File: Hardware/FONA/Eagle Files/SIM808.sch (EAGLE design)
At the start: 28 parts, among them SW1 KMR2, SW2 KMR2, X2 uFL, X3 uFL, X6 SIM_LOCKAMPHENOL

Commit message: Corrige el esquemático para el SIM808
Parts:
- removed R4, R6: 10K, microbuilder:RESISTOR0805_NOOUTLINE
- removed X2: uFL, microbuilder:SMACONNECTOR_EDGE_UFL
- added D7: 1N4148, microbuilder:DIODESOD-323
- added R1: 10K, microbuilder:RESISTOR0805_NOOUTLINE
- added X1: uFL, microbuilder:ANTENNA_U.FL
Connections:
- new net N$2: D7.A, U1.RI
- new net RI_P: D7.C, R1.2
- net GND: now also R1.1, X1.GND@0, X1.GND@1; no longer R4.1, R6.1, X2.GND1, X2.GND2, X2.GND3, X2.GND4
- net N$16: now also X1.SIGNAL; no longer X2.ANT
- net NS_P: no longer R4.2
- net PS_P: no longer R6.2
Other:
- moved on the sheet: D1, D3, D4, R2, R7, SW1, SW2

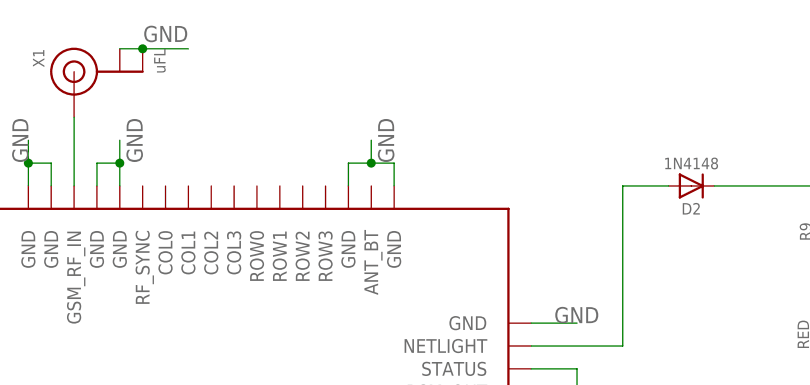
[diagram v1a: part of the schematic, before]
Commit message: Agrega antena para BT en SIM808
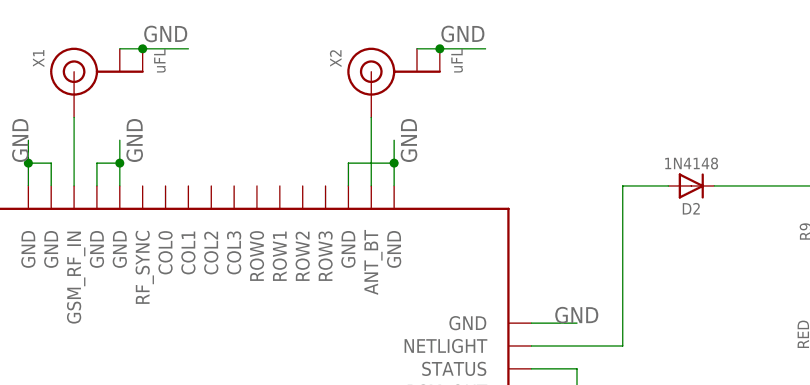
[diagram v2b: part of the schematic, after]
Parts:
- added X2: uFL, microbuilder:ANTENNA_U.FL
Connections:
- new net N$4: X2.SIGNAL
- net GND: now also X2.GND@0, X2.GND@1
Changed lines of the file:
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@@
 <grid distance="0.1" unitdist="inch" unit="inch" style="lines" multiple="1" display="no" altdistance="0.01" altunitdist="inch" altunit="inch"/>
 <layers>
-<layer number="1" name="Top" color="4" fill="1" visible="yes" active="no"/>
-<layer number="16" name="Bottom" color="1" fill="1" visible="yes" active="no"/>
-<layer number="17" name="Pads" color="2" fill="1" visible="yes" active="no"/>
-<layer number="18" name="Vias" color="2" fill="1" visible="yes" active="no"/>
-<layer number="19" name="Unrouted" color="6" fill="1" visible="yes" active="no"/>
-<layer number="20" name="Dimension" color="15" fill="1" visible="yes" active="no"/>
-<layer number="21" name="tPlace" color="7" fill="1" visible="yes" active="no"/>
-<layer number="22" name="bPlace" color="7" fill="1" visible="yes" active="no"/>
-<layer number="23" name="tOrigins" color="15" fill="1" visible="yes" active="no"/>
-<layer number="24" name="bOrigins" color="15" fill="1" visible="yes" active="no"/>
-<layer number="25" name="tNames" color="7" fill="1" visible="yes" active="no"/>
-<layer number="26" name="bNames" color="7" fill="1" visible="yes" active="no"/>
-<layer number="27" name="tValues" color="7" fill="1" visible="yes" active="no"/>
-<layer number="28" name="bValues" color="7" fill="1" visible="yes" active="no"/>
+<layer number="1" name="Top" color="4" fill="1" visible="no" active="no"/>
+<layer number="16" name="Bottom" color="1" fill="1" visible="no" active="no"/>
+<layer number="17" name="Pads" color="2" fill="1" visible="no" active="no"/>
+<layer number="18" name="Vias" color="2" fill="1" visible="no" active="no"/>
+<layer number="19" name="Unrouted" color="6" fill="1" visible="no" active="no"/>
+<layer number="20" name="Dimension" color="15" fill="1" visible="no" active="no"/>
+<layer number="21" name="tPlace" color="7" fill="1" visible="no" active="no"/>
+<layer number="22" name="bPlace" color="7" fill="1" visible="no" active="no"/>
+<layer number="23" name="tOrigins" color="15" fill="1" visible="no" active="no"/>
+<layer number="24" name="bOrigins" color="15" fill="1" visible="no" active="no"/>
+<layer number="25" name="tNames" color="7" fill="1" visible="no" active="no"/>
+<layer number="26" name="bNames" color="7" fill="1" visible="no" active="no"/>
+<layer number="27" name="tValues" color="7" fill="1" visible="no" active="no"/>
+<layer number="28" name="bValues" color="7" fill="1" visible="no" active="no"/>
 <layer number="29" name="tStop" color="7" fill="3" visible="no" active="no"/>
 <layer number="30" name="bStop" color="7" fill="6" visible="no" active="no"/>
@@
 <layer number="35" name="tGlue" color="7" fill="4" visible="no" active="no"/>
 <layer number="36" name="bGlue" color="7" fill="5" visible="no" active="no"/>
-<layer number="37" name="tTest" color="7" fill="1" visible="yes" active="no"/>
-<layer number="38" name="bTest" color="7" fill="1" visible="yes" active="no"/>
+<layer number="37" name="tTest" color="7" fill="1" visible="no" active="no"/>
+<layer number="38" name="bTest" color="7" fill="1" visible="no" active="no"/>
 <layer number="39" name="tKeepout" color="4" fill="11" visible="no" active="no"/>
 <layer number="40" name="bKeepout" color="1" fill="11" visible="no" active="no"/>
@@
 <layer number="44" name="Drills" color="7" fill="1" visible="no" active="no"/>
 <layer number="45" name="Holes" color="7" fill="1" visible="no" active="no"/>
-<layer number="46" name="Milling" color="3" fill="1" visible="yes" active="no"/>
-<layer number="47" name="Measures" color="7" fill="1" visible="yes" active="no"/>
-<layer number="48" name="Document" color="7" fill="1" visible="yes" active="no"/>
-<layer number="49" name="Reference" color="7" fill="1" visible="yes" active="no"/>
-<layer number="50" name="dxf" color="7" fill="1" visible="yes" active="no"/>
-<layer number="51" name="tDocu" color="7" fill="1" visible="yes" active="no"/>
-<layer number="52" name="bDocu" color="7" fill="1" visible="yes" active="no"/>
-<layer number="53" name="tGND_GNDA" color="7" fill="9" visible="yes" active="no"/>
-<layer number="54" name="bGND_GNDA" color="1" fill="9" visible="yes" active="no"/>
-<layer number="56" name="wert" color="7" fill="1" visible="yes" active="no"/>
-<layer number="57" name="tCAD" color="7" fill="1" visible="yes" active="no"/>
-<layer number="59" name="tCarbon" color="7" fill="1" visible="yes" active="no"/>
-<layer number="60" name="bCarbon" color="7" fill="1" visible="yes" active="no"/>
+<layer number="46" name="Milling" color="3" fill="1" visible="no" active="no"/>
+<layer number="47" name="Measures" color="7" fill="1" visible="no" active="no"/>
+<layer number="48" name="Document" color="7" fill="1" visible="no" active="no"/>
+<layer number="49" name="Reference" color="7" fill="1" visible="no" active="no"/>
+<layer number="50" name="dxf" color="7" fill="1" visible="no" active="no"/>
+<layer number="51" name="tDocu" color="7" fill="1" visible="no" active="no"/>
+<layer number="52" name="bDocu" color="7" fill="1" visible="no" active="no"/>
+<layer number="53" name="tGND_GNDA" color="7" fill="9" visible="no" active="no"/>
+<layer number="54" name="bGND_GNDA" color="1" fill="9" visible="no" active="no"/>
+<layer number="56" name="wert" color="7" fill="1" visible="no" active="no"/>
+<layer number="57" name="tCAD" color="7" fill="1" visible="no" active="no"/>
+<layer number="59" name="tCarbon" color="7" fill="1" visible="no" active="no"/>
+<layer number="60" name="bCarbon" color="7" fill="1" visible="no" active="no"/>
 <layer number="90" name="Modules" color="5" fill="1" visible="yes" active="yes"/>
 <layer number="91" name="Nets" color="2" fill="1" visible="yes" active="yes"/>
@@
 <part name="D7" library="microbuilder" deviceset="DIODE" device="SOD-323" value="1N4148"/>
 <part name="R1" library="microbuilder" deviceset="RESISTOR" device="0805_NOOUTLINE" value="10K"/>
+<part name="X2" library="microbuilder" deviceset="ANTENNA_U.FL" device="" value="uFL"/>
 </parts>
 <sheets>
@@
 <instance part="D7" gate="G$1" x="15.24" y="48.26" rot="MR0"/>
 <instance part="R1" gate="G$1" x="7.62" y="40.64" rot="R90"/>
+<instance part="X2" gate="G$1" x="93.98" y="93.98" rot="MR270"/>
 </instances>
 <busses>
@@
 <wire x1="96.52" y1="81.28" x2="96.52" y2="83.82" width="0.1524" layer="91"/>
 <pinref part="U1" gate="G$1" pin="GND@11"/>
-<wire x1="96.52" y1="83.82" x2="93.98" y2="83.82" width="0.1524" layer="91"/>
-<wire x1="93.98" y1="83.82" x2="91.44" y2="83.82" width="0.1524" layer="91"/>
+<wire x1="96.52" y1="83.82" x2="91.44" y2="83.82" width="0.1524" layer="91"/>
 <wire x1="91.44" y1="83.82" x2="91.44" y2="81.28" width="0.1524" layer="91"/>
-<wire x1="93.98" y1="83.82" x2="93.98" y2="86.36" width="0.1524" layer="91"/>
-<junction x="93.98" y="83.82"/>
-<label x="96.52" y="83.82" size="1.778" layer="95" rot="R90"/>
+<wire x1="96.52" y1="83.82" x2="96.52" y2="86.36" width="0.1524" layer="91"/>
+<junction x="96.52" y="83.82"/>
+<label x="99.06" y="83.82" size="1.778" layer="95" rot="R90"/>
 </segment>
 <segment>
@@
 <label x="7.62" y="33.02" size="1.778" layer="95"/>
 <pinref part="R1" gate="G$1" pin="1"/>
+</segment>
+<segment>
+<pinref part="X2" gate="G$1" pin="GND@1"/>
+<pinref part="X2" gate="G$1" pin="GND@0"/>
+<wire x1="99.06" y1="96.52" x2="101.6" y2="96.52" width="0.1524" layer="91"/>
+<junction x="101.6" y="96.52"/>
+<wire x1="101.6" y1="96.52" x2="106.68" y2="96.52" width="0.1524" layer="91"/>
+<label x="106.68" y="99.06" size="1.778" layer="95" rot="R180"/>
 </segment>
 </net>
@@
 </segment>
 </net>
+<net name="N$4" class="0">
+<segment>
+<wire x1="93.98" y1="88.9" x2="93.98" y2="81.28" width="0.1524" layer="91"/>
+<pinref part="X2" gate="G$1" pin="SIGNAL"/>
+</segment>
+</net>
